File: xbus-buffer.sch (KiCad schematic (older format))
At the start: 4 parts, among them IC12 74LS245, IC15 74LS244, IC16 74LS244, IC18 74LS244

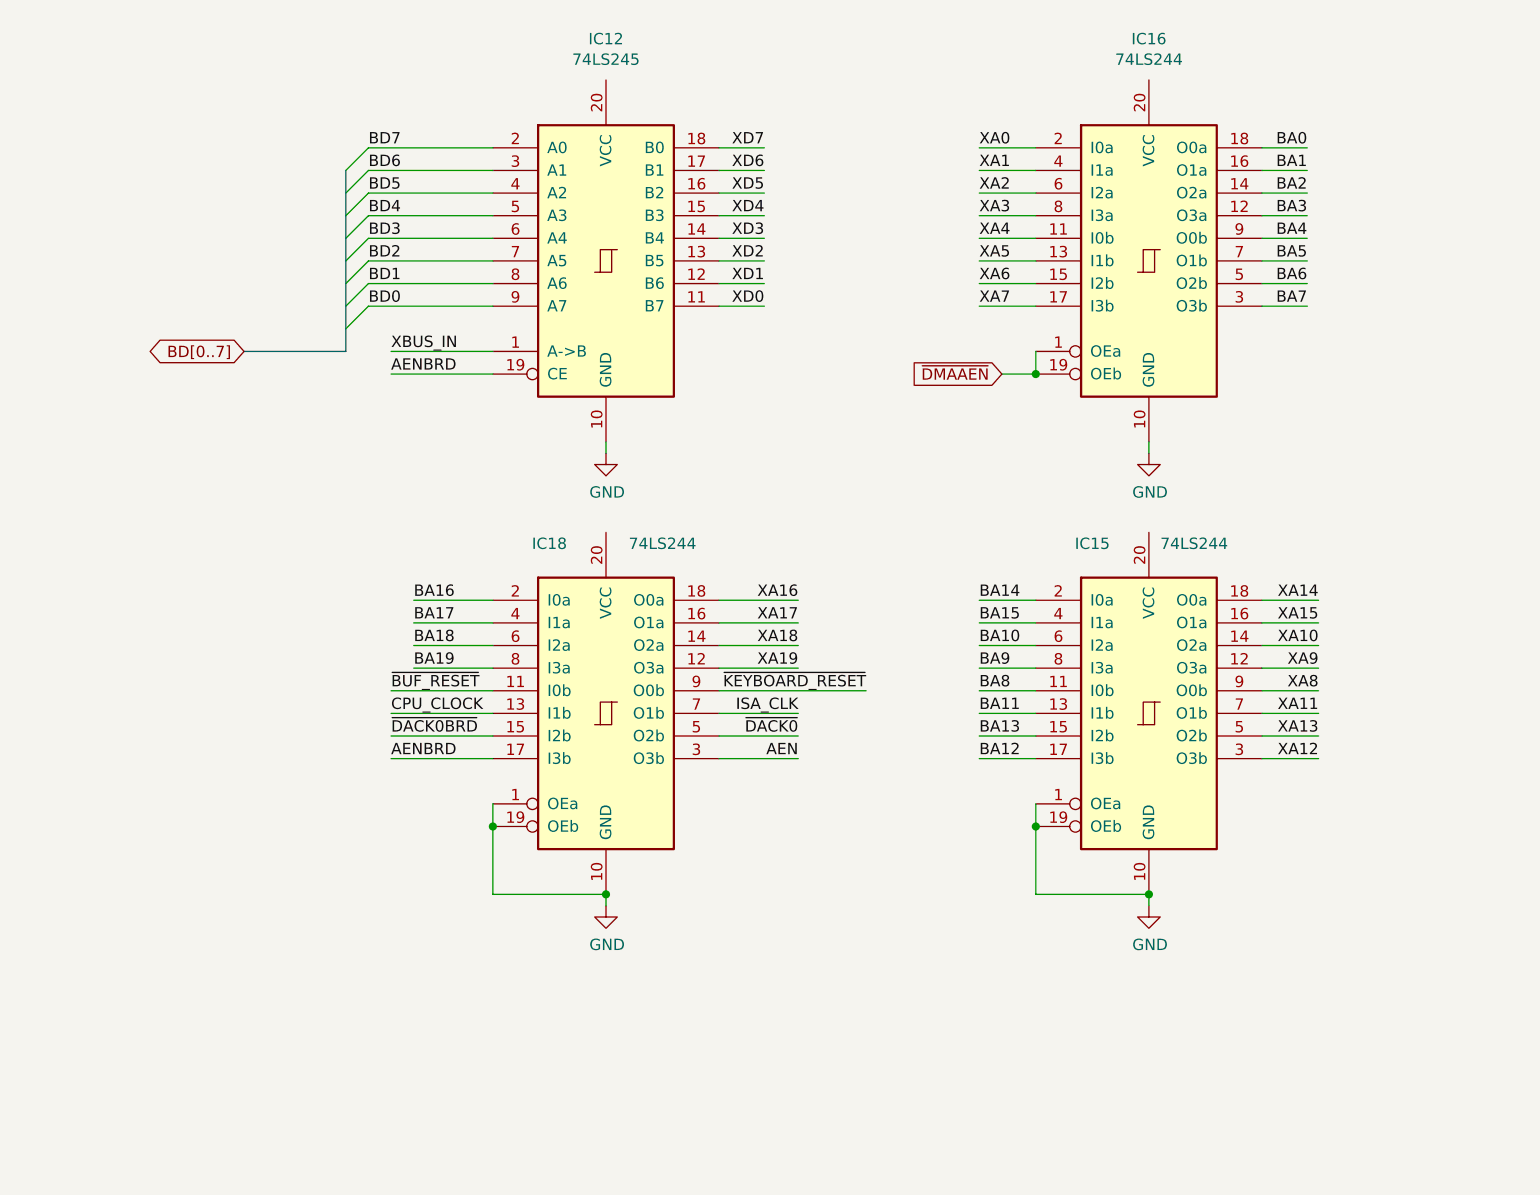
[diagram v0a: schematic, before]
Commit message: Tidy up and map all signals
This fixes up the schematic to:
 - Look presentable
 - Fix all labels connecting sheets
 - Tidy up all loose ends by either inspecting the PCB under
    magnification, measuring with an oscillosope or buzzing
    out with a meter
 - Pass ERC (with 1 exception due to incorrect circuitry around
    pin 33 on the FPU (~RQ~/~GT1~)
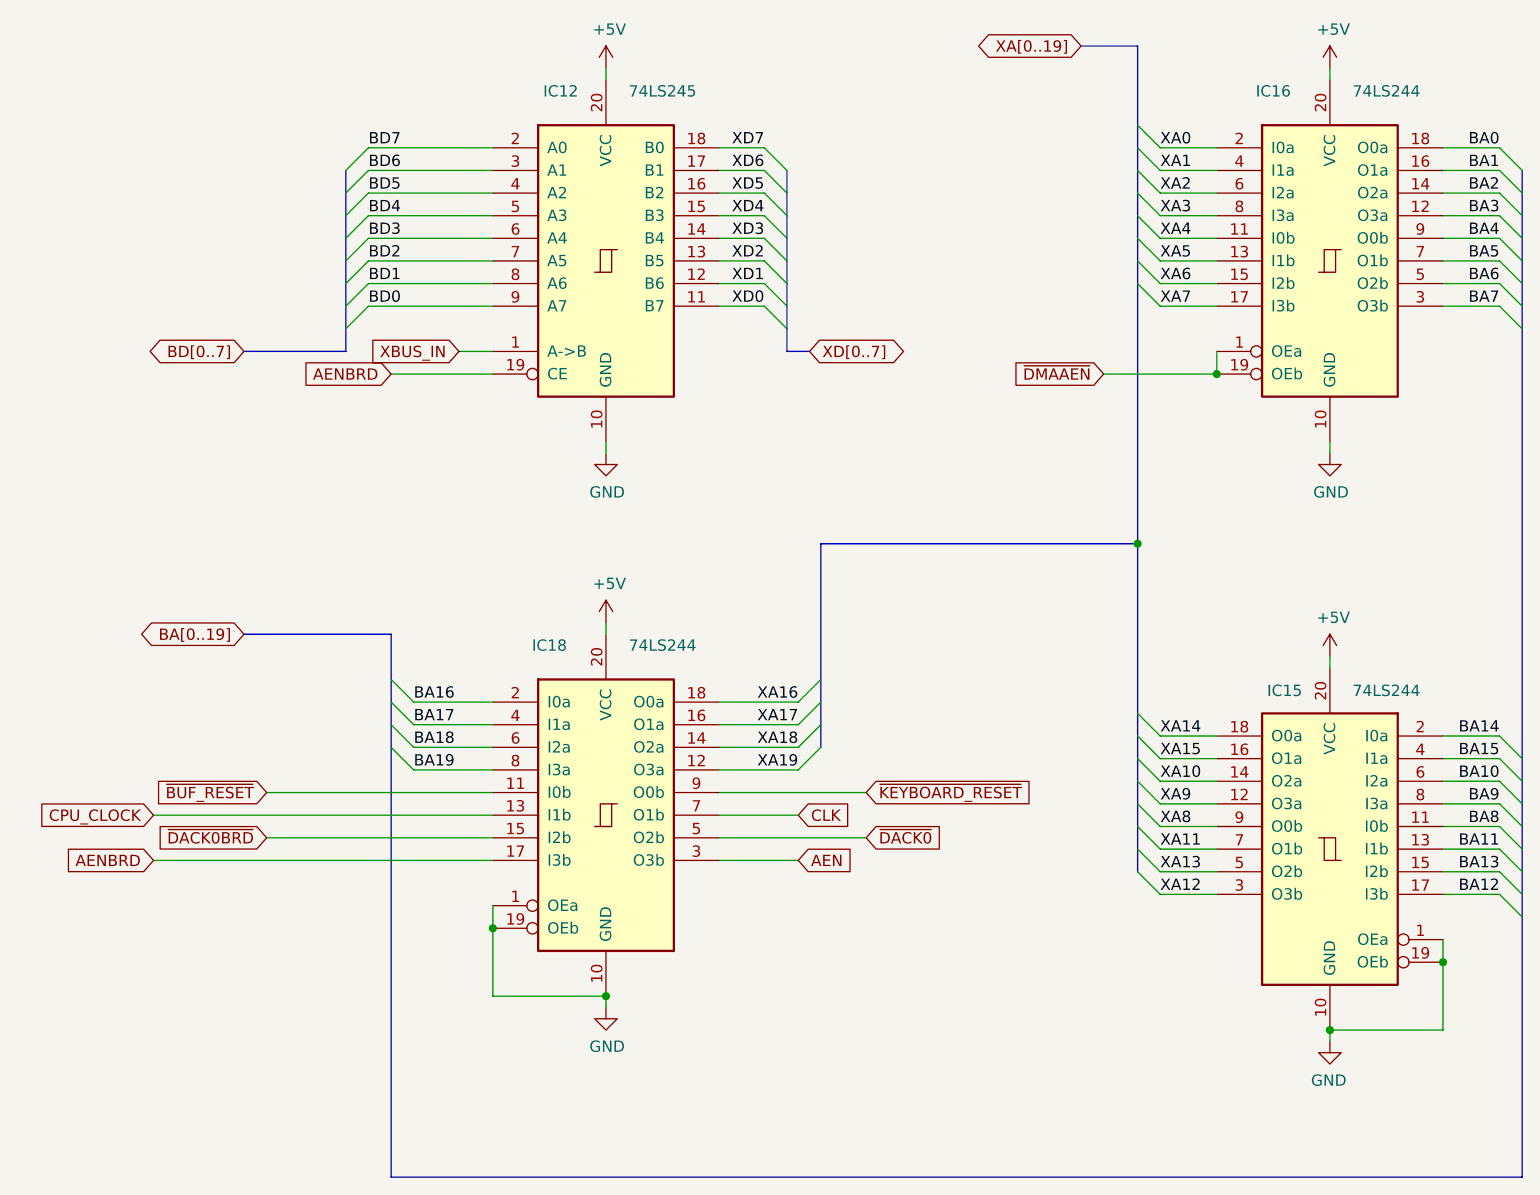
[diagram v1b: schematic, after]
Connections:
- net +5V: now reaches IC12.20 (VCC)
- net +5V: now also IC15.20 (VCC), IC16.20 (VCC), IC18.20 (VCC)
- net ISA_CLK renamed CLK
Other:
- moved on the sheet: IC15, IC16, IC18
